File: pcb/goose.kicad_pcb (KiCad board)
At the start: 2 copper layers, 131.7 x 96.3 mm, 47 parts

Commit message: Ok version
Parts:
- _1: moved to B.Cu
- moved BAT1 47.2 mm to (251.6, 111.0)
- moved ROT1 3.01 mm to (282.1, 159.4)
- moved D6 1.00 mm to (190.7, 122.8)
- moved D15 1.00 mm to (254.1, 124.7)
- moved D19 1.00 mm to (271.4, 185.8)
- moved D1 1.00 mm to (173.4, 170.5)
- moved D2 1.00 mm to (171.3, 151.6)
- moved D18 1.00 mm to (251.4, 182.4)
- moved D16 1.00 mm to (212.4, 173.7)
- moved D7 1.00 mm to (212.2, 154.6)
- moved D9 1.00 mm to (211.9, 116.6)
- moved D8 1.00 mm to (212.1, 135.6)
- moved D13 1.00 mm to (252.4, 162.6)
- moved D4 1.00 mm to (192.4, 160.8)
- moved D5 1.00 mm to (191.6, 141.8)
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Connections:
- BAT1 pad 2: BAT- -> GND
- ROT1 pad A: P7 -> P9
- ROT1 pad B: P8 -> P10
- _1 pad : (no net) -> BAT+
- _1 pad 1: R0 -> P0
- _1 pad 10: C3 -> P9
- _1 pad 11: C4 -> P10
- _1 pad 2: R1 -> P1
- _1 pad 3: R2 -> P2
- _1 pad 4: R3 -> P3
- _1 pad 5: C0 -> P4
- _1 pad 6: C1 -> P5
- _1 pad 7: C2 -> P6

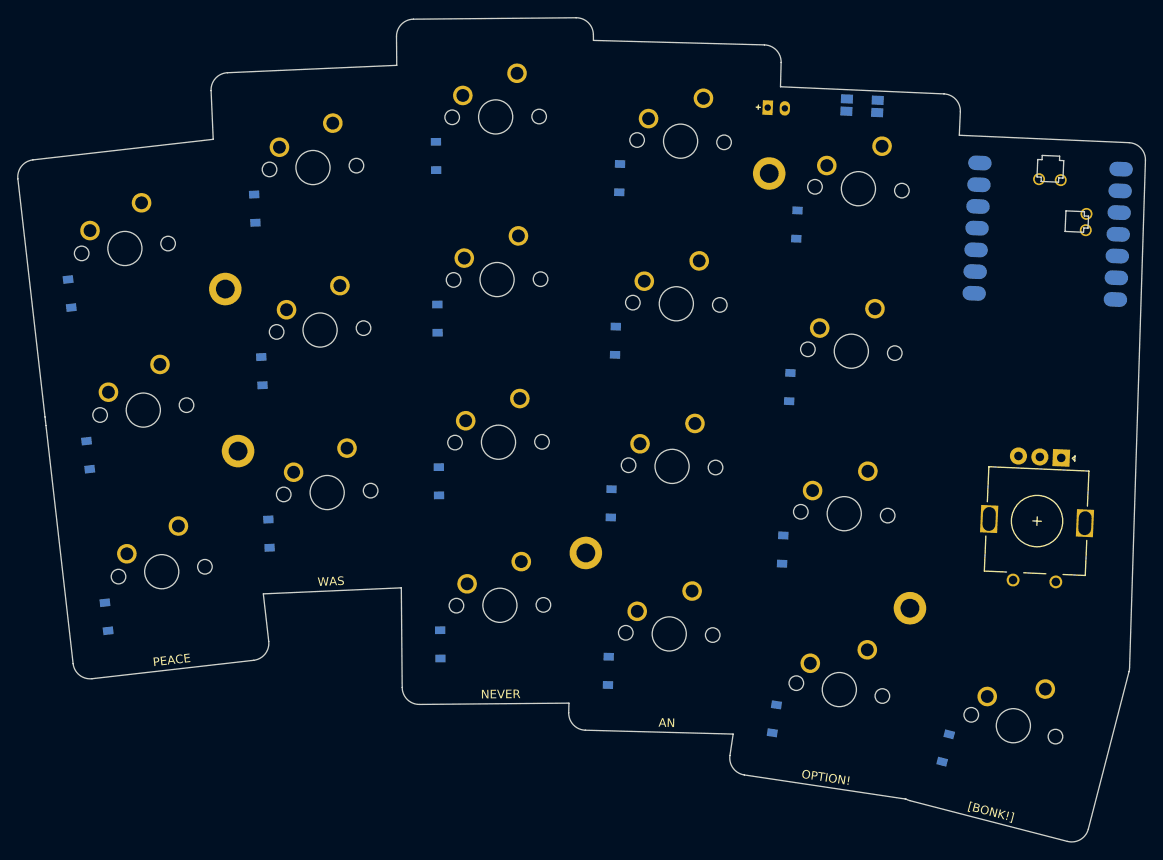
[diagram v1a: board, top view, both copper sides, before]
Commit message: Mirrored pcbs
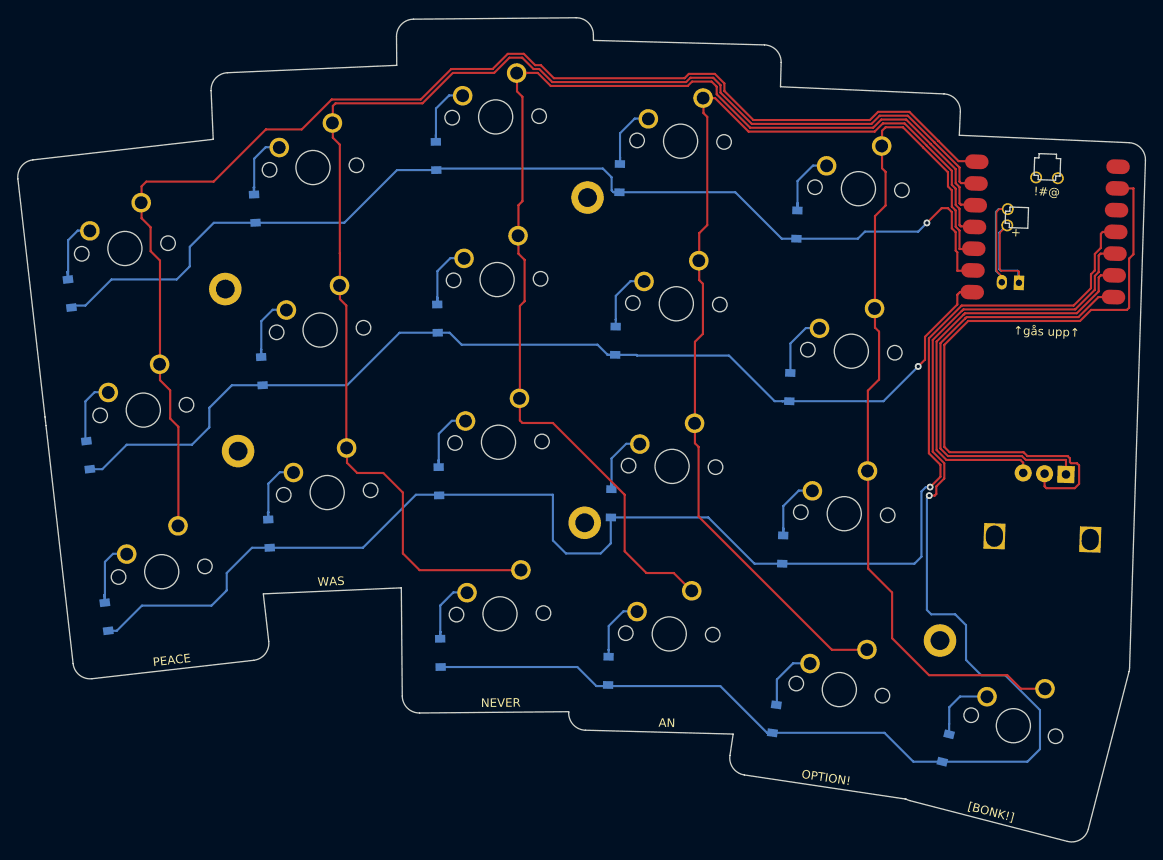
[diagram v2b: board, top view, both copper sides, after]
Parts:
- removed D1, D10, D11, D12, D13, D14, D15, D16, D17, D18, D19, D2, D3, D4, D5, D6, D7, D8, D9: , Diode_SMD:D_SOD-123
- removed SW1: , sw_reset_side
- added Di1: , Diode_SMD:D_SOD-123, B.Cu at (254.1, 124.7)
- added Di10: , Diode_SMD:D_SOD-123, B.Cu at (232.4, 157.2)
- added Di11: , Diode_SMD:D_SOD-123, B.Cu at (191.6, 141.8)
- added Di12: , Diode_SMD:D_SOD-123, B.Cu at (212.2, 154.6)
- added Di13: , Diode_SMD:D_SOD-123, B.Cu at (192.4, 160.8)
- added Di14: , Diode_SMD:D_SOD-123, B.Cu at (171.3, 151.6)
- added Di15: , Diode_SMD:D_SOD-123, B.Cu at (271.4, 185.8)
- added Di16: , Diode_SMD:D_SOD-123, B.Cu at (251.4, 182.4)
- added Di17: , Diode_SMD:D_SOD-123, B.Cu at (232.0, 176.8)
- added Di18: , Diode_SMD:D_SOD-123, B.Cu at (212.4, 174.7)
- added Di19: , Diode_SMD:D_SOD-123, B.Cu at (173.4, 170.5)
- added Di2: , Diode_SMD:D_SOD-123, B.Cu at (232.9, 138.2)
- added Di3: , Diode_SMD:D_SOD-123, B.Cu at (233.4, 119.2)
- added Di4: , Diode_SMD:D_SOD-123, B.Cu at (190.7, 122.8)
- added Di5: , Diode_SMD:D_SOD-123, B.Cu at (212.1, 135.6)
- added Di6: , Diode_SMD:D_SOD-123, B.Cu at (211.9, 116.6)
- added Di7: , Diode_SMD:D_SOD-123, B.Cu at (169.1, 132.7)
- added Di8: , Diode_SMD:D_SOD-123, B.Cu at (252.4, 162.6)
- added Di9: , Diode_SMD:D_SOD-123, B.Cu at (253.2, 143.6)
- BAT1: moved to B.Cu
- ROT1: footprint rotary_encoder -> Rotary_Encoder:RotaryEncoder_Alps_EC12E_Vertical_H20mm
- _1: moved to F.Cu
- moved S15 92.9 mm to (179.9, 165.2), turned to 7 degrees
- moved H3 70.0 mm to (188.8, 151.1), turned to 5 degrees
- moved S1 65.9 mm to (218.9, 112.1), turned to 1 degrees
- moved S10 62.1 mm to (177.7, 146.3), turned to 7 degrees
- moved H2 50.4 mm to (229.6, 121.5), turned to 0 degrees
- moved S11 46.4 mm to (199.2, 156.0), turned to 3 degrees
- moved S6 45.3 mm to (240.0, 133.9), turned to -1 degrees
- moved S9 43.2 mm to (261.2, 120.5), turned to -2 degrees
- moved S8 42.2 mm to (260.4, 139.4), turned to -2 degrees
- moved S13 41.2 mm to (219.2, 150.1), turned to 1 degrees
- moved S7 41.1 mm to (240.5, 114.9), turned to -1 degrees
- moved S12 38.0 mm to (239.5, 152.9), turned to -1 degrees
- moved S4 38.0 mm to (197.5, 118.0), turned to 3 degrees
- moved BAT1 34.1 mm to (279.0, 131.4), turned to 178 degrees
- moved S3 24.7 mm to (198.4, 137.0), turned to 3 degrees
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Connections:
- net BAT+ renamed BATP
- BAT1 pad 2: GND -> BATN
- ROT1 pad A: P9 -> P7
- ROT1 pad B: P10 -> P8
- S1 pad 1: C0 -> C2
- S1 pad 2: C0_R2 -> C2_R0
- S10 pad 1: C3 -> C0
- S10 pad 2: C3_R2 -> C0_R1
- S11 pad 1: C3 -> C1
- S11 pad 2: C3_R1 -> C1_R2
- S12 pad 2: C3_R0 -> C3_R2
- S13 pad 1: C4 -> C2
- S13 pad 2: C4_R2 -> C2_R2
- S14 pad 2: C4_R1 -> C4_R2
- S15 pad 1: C4 -> C0
- S15 pad 2: C4_R0 -> C0_R2
- S16 pad 1: C1 -> C2
- S16 pad 2: C1_R3 -> C2_R3
- S17 pad 1: C2 -> C1
- S17 pad 2: C2_R3 -> C1_R3
- S2 pad 2: C0_R1 -> C0_R0
- S3 pad 1: C0 -> C1
- S3 pad 2: C0_R0 -> C1_R1
- S4 pad 2: C1_R2 -> C1_R0
- S5 pad 1: C1 -> C2
- S5 pad 2: C1_R1 -> C2_R1
- S6 pad 1: C1 -> C3
- S6 pad 2: C1_R0 -> C3_R1
- S7 pad 1: C2 -> C3
- S7 pad 2: C2_R2 -> C3_R0
- S8 pad 1: C2 -> C4
- S8 pad 2: C2_R1 -> C4_R1
- S9 pad 1: C2 -> C4
- S9 pad 2: C2_R0 -> C4_R0
- _1 pad 1: P0 -> C0
- _1 pad 10: P9 -> R3
- _1 pad 11: P10 -> R2
- _1 pad 2: P1 -> C1
- _1 pad 3: P2 -> C2
- _1 pad 4: P3 -> C3
- _1 pad 5: P4 -> C4
- _1 pad 6: P5 -> R0
- _1 pad 7: P6 -> R1
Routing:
- net R2: track 0.00 -> 172.1 mm, vias 0 -> 1
- net R3: track 0.00 -> 161.1 mm, vias 0 -> 1
- net C1: track 0.00 -> 158.6 mm
- net C0: track 0.00 -> 153.5 mm
- net C2: track 0.00 -> 137.4 mm
- net R0: track 0.00 -> 125.2 mm, vias 0 -> 1
- net R1: track 0.00 -> 123.5 mm, vias 0 -> 1
- net C3: track 0.00 -> 118.1 mm
- net C4: track 0.00 -> 102.7 mm
- net GND: track 0.00 -> 76.2 mm
- net P7: track 0.00 -> 51.7 mm
- net P8: track 0.00 -> 49.5 mm
- net BATN: track 0.00 -> 18.5 mm
- net BATP: track 0.00 -> 18.3 mm
- net C1_R1: track 0.00 -> 8.92 mm
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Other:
- outline, holes or cut-outs redrawn
- board text added: "!#@"
- board text added: "+"
- board text added: "gooses v0.8a"
- board text added: "↑gås upp↑"
- board text added: "↓gås ner↓"
